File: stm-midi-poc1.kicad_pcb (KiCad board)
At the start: 4 copper layers, 100 x 100 mm, 116 parts, among them CN1 MIDI Out 1, CN2 MIDI In 1, CN3 MIDI Out 2, CN4 MIDI In 2, CN5 Line out, CN6 Headphone, J1 GT-USB-7010I, J2 SWD, J3 I2C, J4 UART456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

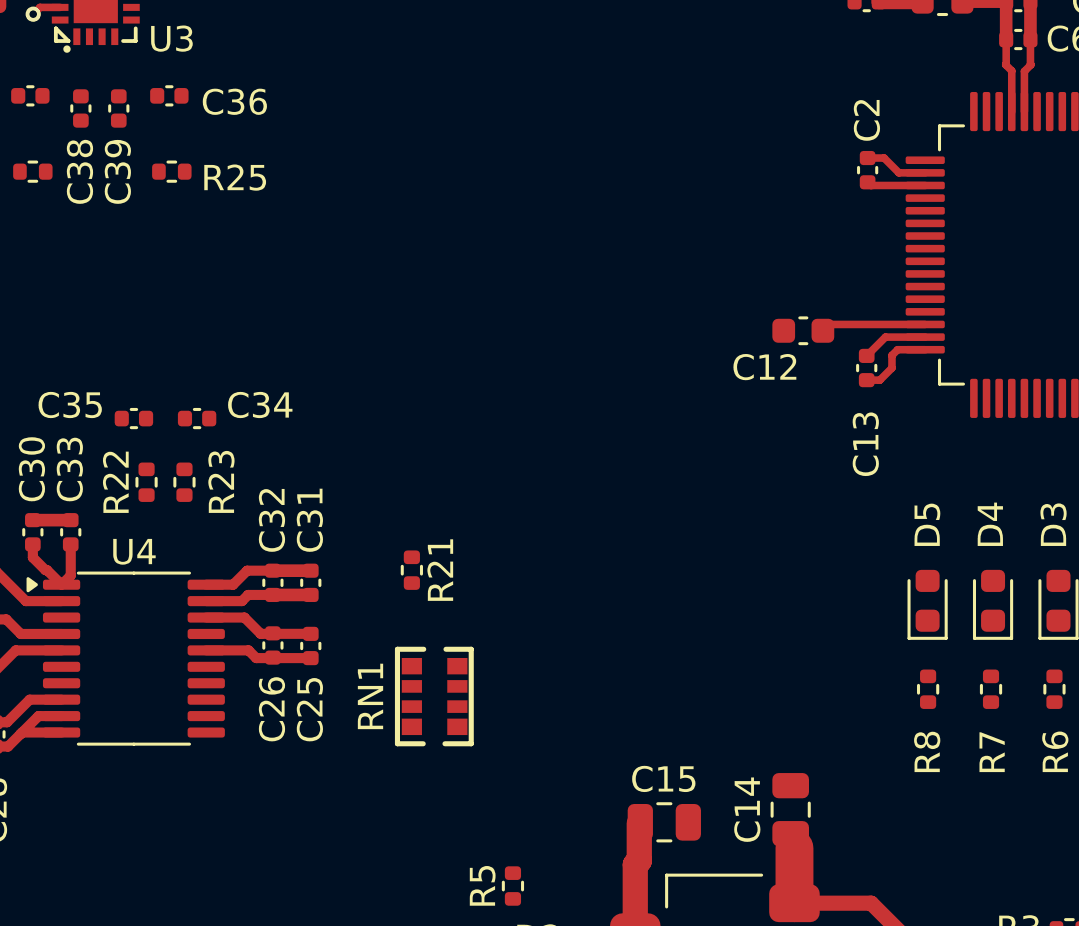
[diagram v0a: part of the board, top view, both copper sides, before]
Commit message: Routed DAC digital signals
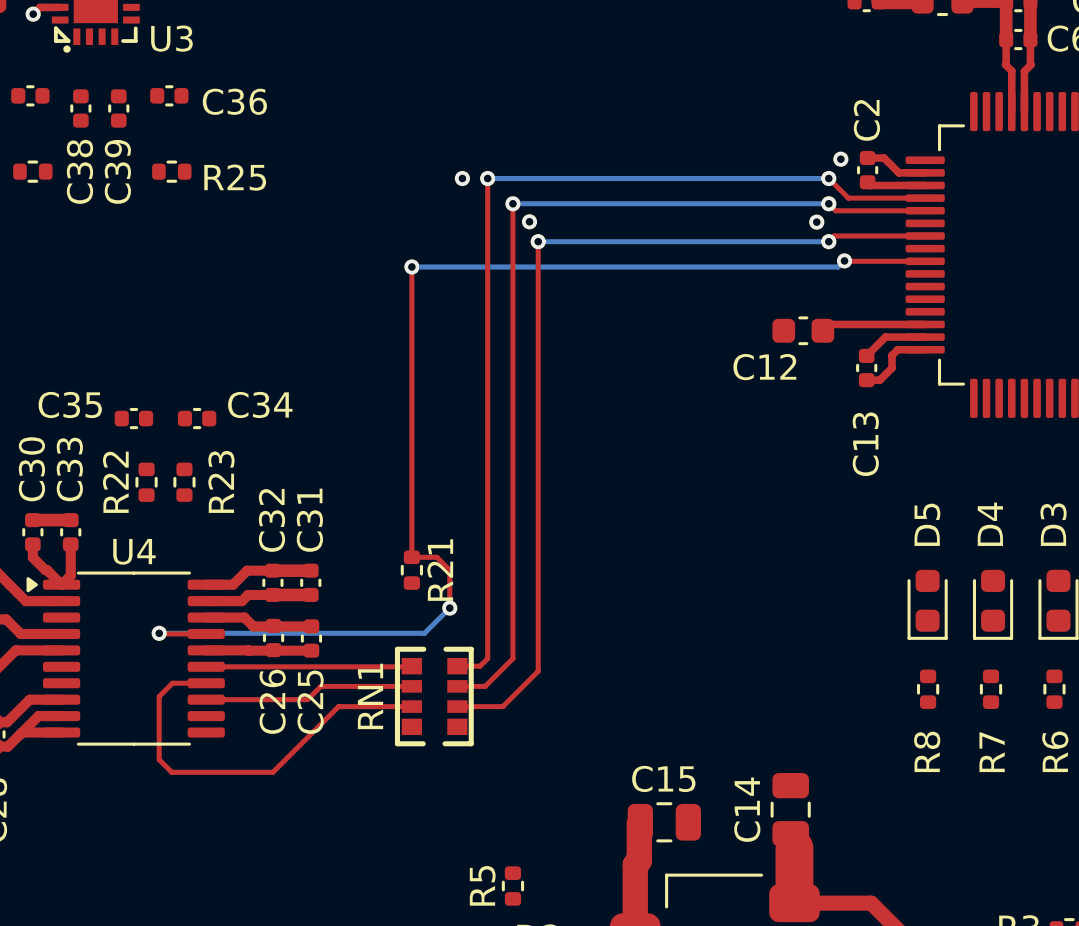
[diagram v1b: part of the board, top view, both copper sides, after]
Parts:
- moved C26 0.30 mm to (139.5, 115.2)
- moved C25 0.30 mm to (141.0, 115.2)
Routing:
- net AUDIO_MUTE: track 0.00 -> 48.9 mm, vias 0 -> 4
- net I2S1_WS: track 0.00 -> 38.0 mm, vias 0 -> 2
- net I2S1_CK: track 0.00 -> 37.1 mm, vias 0 -> 2
- net I2S1_SD: track 0.00 -> 36.2 mm, vias 0 -> 2
- net /Audio Output/DAC_SD: track 0.00 -> 15.9 mm
- net /Audio Output/DAC_CK: track 0.00 -> 8.35 mm
- net /Audio Output/DAC_WS: track 0.00 -> 8.15 mm
- net GND: track 83.0 -> 82.9 mm, vias 13 -> 17

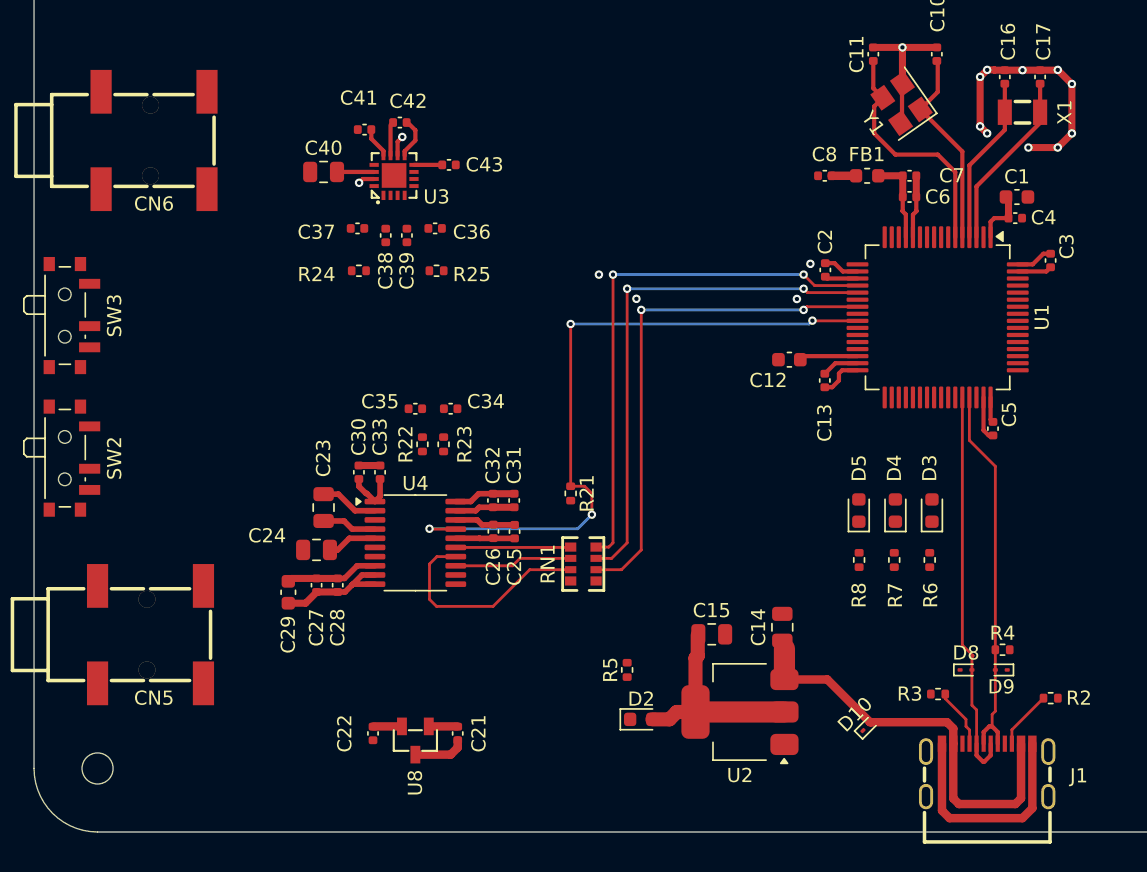
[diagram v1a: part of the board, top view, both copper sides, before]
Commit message: Added GND routing for DAC, USB, power areas
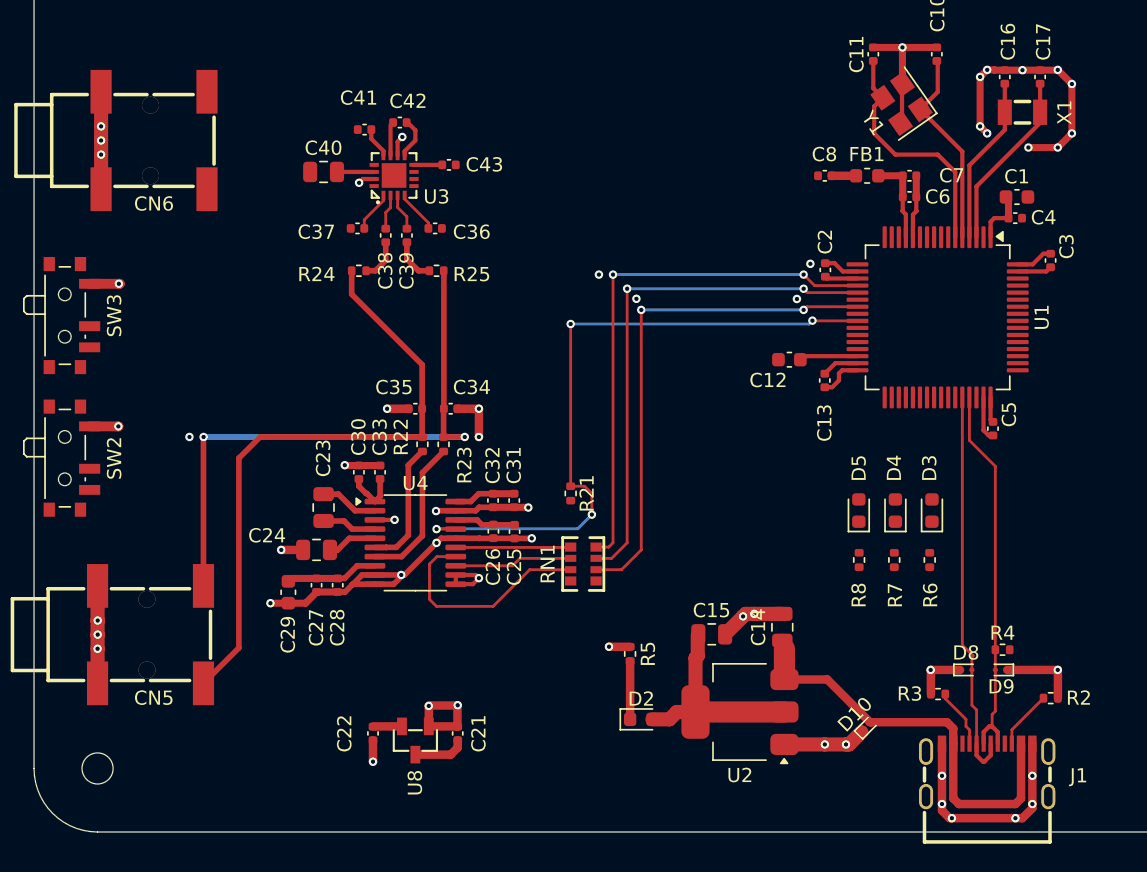
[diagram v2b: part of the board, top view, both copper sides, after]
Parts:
- moved R5 1.15 mm to (149.2, 123.9)
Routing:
- net GND: track 82.9 -> 156.0 mm, vias 17 -> 55
- net LINE_L: track 0.00 -> 44.5 mm
- net LINE_R: track 0.00 -> 42.4 mm, vias 0 -> 2
- net /Audio Output/DAC_OUT_R: track 0.00 -> 10.6 mm
- net /Audio Output/DAC_OUT_L: track 0.00 -> 9.08 mm
- net /MCU/PWR_LED_K: track 0.00 -> 4.12 mm
- net /Audio Output/INR+_CR: track 0.00 -> 3.12 mm
- net /Audio Output/HPA_INR-: track 0.00 -> 3.04 mm
- net /Audio Output/INL+_CR: track 0.00 -> 2.98 mm
- net /Audio Output/HPA_INL-: track 0.00 -> 2.90 mm
- net /Audio Output/HPA_INR+: track 0.00 -> 2.63 mm
- net /Audio Output/HPA_INL+: track 0.00 -> 2.50 mm
- net AUDIO_MUTE: track 48.9 -> 47.9 mm

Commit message: Routed Headphone Amplifier
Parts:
- moved C43 0.16 mm to (136.4, 89.1)
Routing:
- net /Audio Output/Gain0: track 0.00 -> 60.2 mm, vias 0 -> 2
- net /Audio Output/Gain1: track 0.00 -> 45.9 mm, vias 0 -> 2
- net AUDIO_MUTE: track 47.9 -> 84.1 mm, vias 4 -> 6
- net HEADPHONE_R: track 0.00 -> 31.6 mm
- net GND: track 156.0 -> 168.8 mm, vias 55 -> 64
- net HEADPHONE_L: track 0.00 -> 12.5 mm

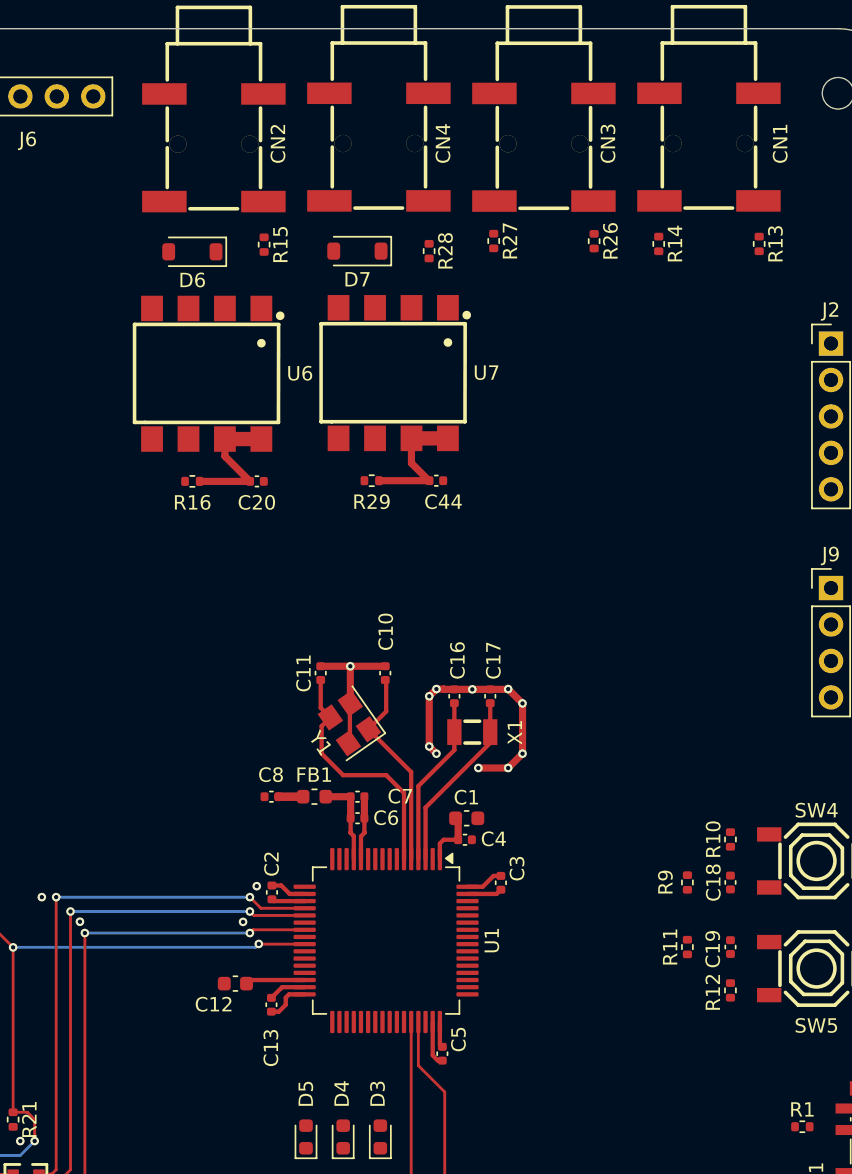
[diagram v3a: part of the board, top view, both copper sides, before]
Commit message: Routed MIDI
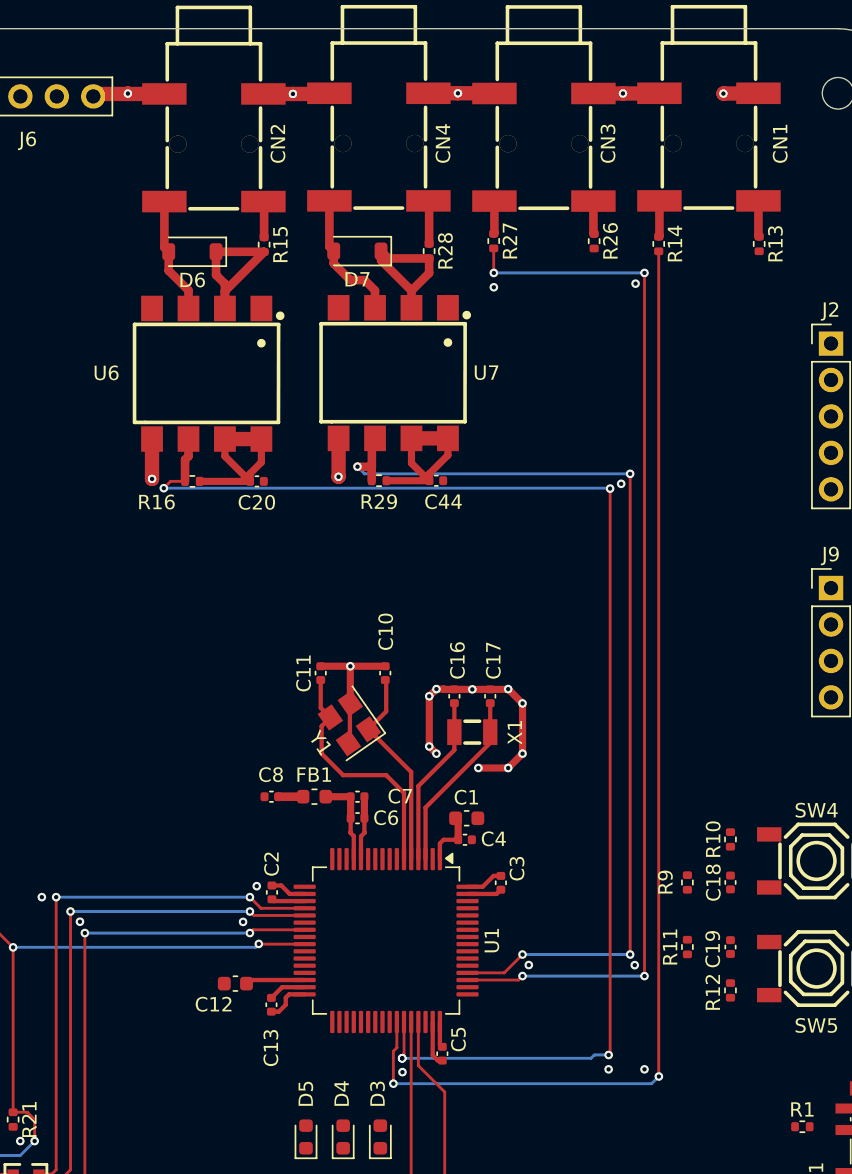
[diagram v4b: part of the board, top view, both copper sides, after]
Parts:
- moved R29 0.51 mm to (170.5, 68.0)
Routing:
- net USART1_RX: track 0.00 -> 92.1 mm, vias 0 -> 5
- net USART1_TX: track 0.00 -> 80.6 mm, vias 0 -> 2
- net USART3_TX: track 0.00 -> 73.7 mm, vias 0 -> 4
- net USART3_RX: track 0.00 -> 68.6 mm, vias 0 -> 4
- net GND: track 168.8 -> 195.6 mm, vias 64 -> 79
- net /MIDI/OI1-SRC: track 0.00 -> 12.6 mm
- net /MIDI/OI2-SRC: track 0.00 -> 11.1 mm
- net /MIDI/MI2-SNK: track 0.00 -> 9.35 mm
- net /MIDI/MI1-SNK: track 0.00 -> 8.15 mm
- net +3V3: track 53.8 -> 60.0 mm
- net /MIDI/MI2-SRC: track 0.00 -> 3.01 mm
- net /MIDI/MI1-SRC: track 0.00 -> 2.51 mm
- net /MIDI/MO1-SRC: track 0.00 -> 2.51 mm
- net /MIDI/MO1-SNK: track 0.00 -> 2.51 mm
- net /MIDI/MO2-SRC: track 0.00 -> 2.30 mm
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
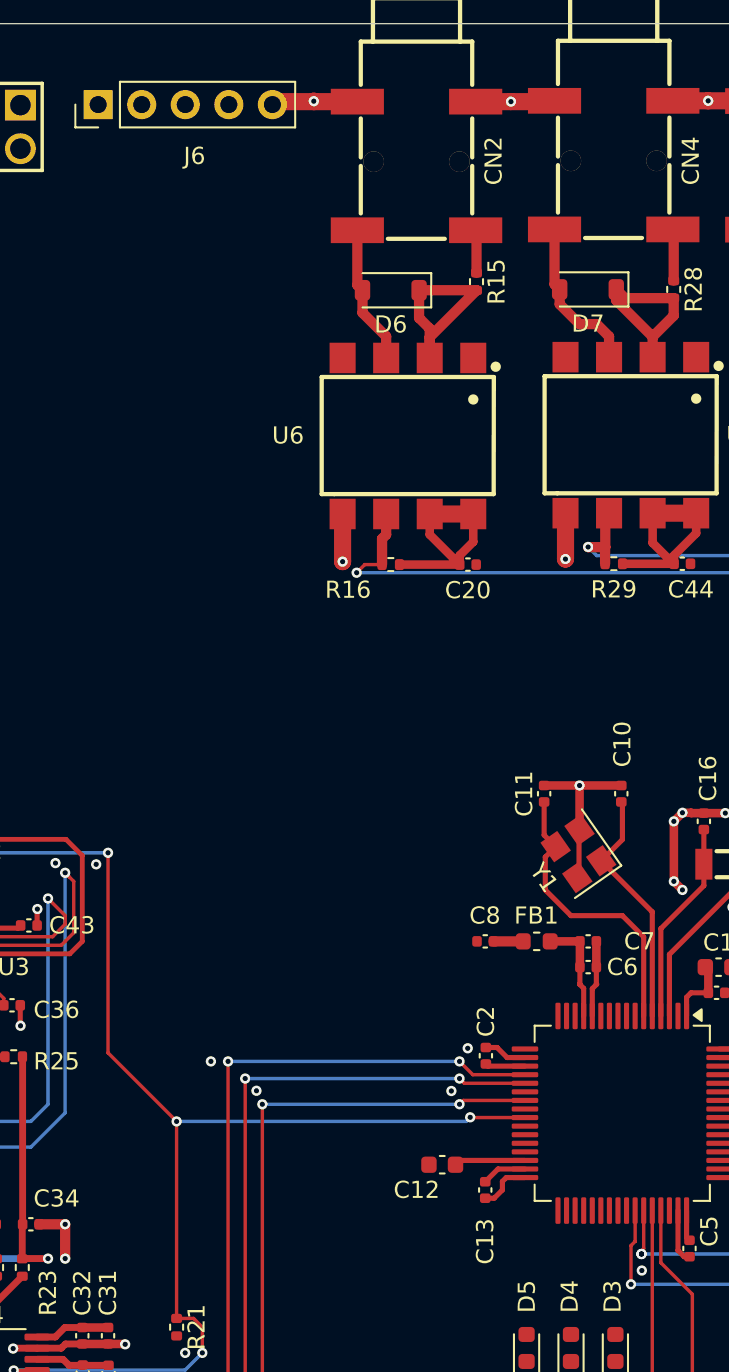
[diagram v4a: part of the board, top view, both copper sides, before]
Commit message: Routed SPI
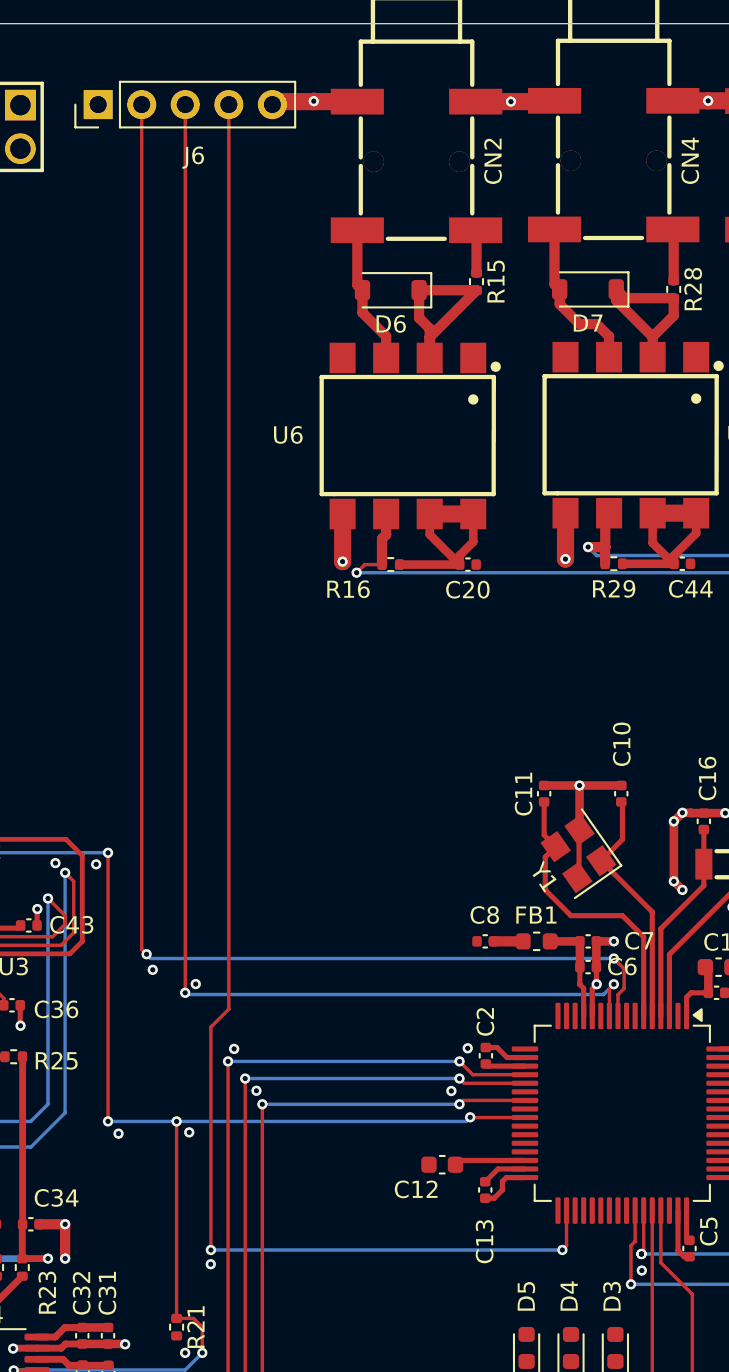
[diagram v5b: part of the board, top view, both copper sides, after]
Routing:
- net SPI2_SCK: track 0.00 -> 90.1 mm, vias 0 -> 2
- net SPI2_MOSI: track 0.00 -> 81.1 mm, vias 0 -> 2
- net SPI2_MISO: track 0.00 -> 79.1 mm, vias 0 -> 2
- net AUDIO_MUTE: track 84.1 -> 86.4 mm, vias 6 -> 7
- net GND: track 195.6 -> 196.7 mm, vias 79 -> 85
- net (no net): vias 0 -> 1
